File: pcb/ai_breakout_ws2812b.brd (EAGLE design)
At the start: 11.4 x 7.6 mm, 5 parts

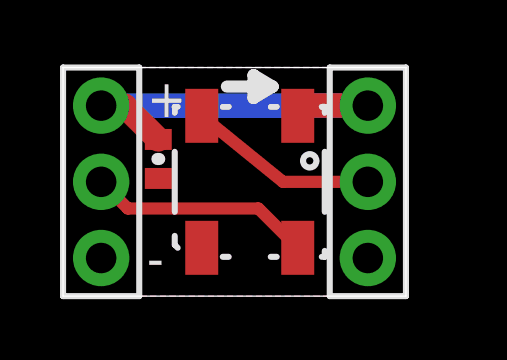
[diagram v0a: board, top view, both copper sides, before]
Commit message: adding panelized version
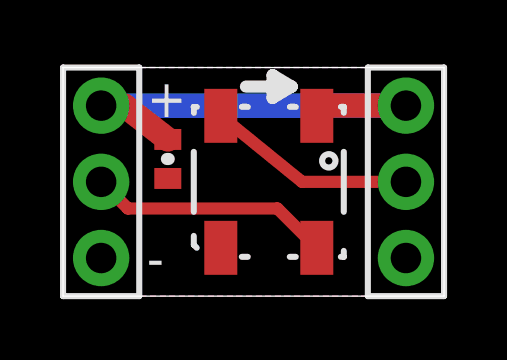
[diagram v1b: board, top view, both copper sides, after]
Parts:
- moved OUT 1.27 mm to (11.4, 3.81)
- moved U$5 0.95 mm to (7.56, 2.67)
- moved RGB 0.63 mm to (6.86, 3.81)
- moved C1 0.32 mm to (3.49, 4.57)
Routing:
- net VCC: track 13.7 -> 15.9 mm
- net DI: track 7.46 -> 8.10 mm
- net DO: track 6.32 -> 6.95 mm
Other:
- board size 11.4 x 7.6 mm -> 12.7 x 7.6 mm
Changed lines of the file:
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@@
 <?xml version="1.0" encoding="utf-8"?>
 <!DOCTYPE eagle SYSTEM "eagle.dtd">
-<eagle version="7.1.0">
+<eagle version="6.5.0">
 <drawing>
 <settings>
@@
 <setting verticaltext="up"/>
 </settings>
-<grid distance="50" unitdist="mil" unit="mil" style="lines" multiple="1" display="yes" altdistance="0.025" altunitdist="inch" altunit="inch"/>
+<grid distance="15" unitdist="mil" unit="mil" style="lines" multiple="1" display="yes" altdistance="0.025" altunitdist="inch" altunit="inch"/>
 <layers>
 <layer number="1" name="Top" color="4" fill="1" visible="yes" active="yes"/>
+<layer number="2" name="Route2" color="1" fill="3" visible="no" active="no"/>
+<layer number="3" name="Route3" color="4" fill="3" visible="no" active="no"/>
+<layer number="4" name="Route4" color="1" fill="4" visible="no" active="no"/>
+<layer number="5" name="Route5" color="4" fill="4" visible="no" active="no"/>
+<layer number="6" name="Route6" color="1" fill="8" visible="no" active="no"/>
+<layer number="7" name="Route7" color="4" fill="8" visible="no" active="no"/>
+<layer number="8" name="Route8" color="1" fill="2" visible="no" active="no"/>
+<layer number="9" name="Route9" color="4" fill="2" visible="no" active="no"/>
+<layer number="10" name="Route10" color="1" fill="7" visible="no" active="no"/>
+<layer number="11" name="Route11" color="4" fill="7" visible="no" active="no"/>
+<layer number="12" name="Route12" color="1" fill="5" visible="no" active="no"/>
+<layer number="13" name="Route13" color="4" fill="5" visible="no" active="no"/>
+<layer number="14" name="Route14" color="1" fill="6" visible="no" active="no"/>
+<layer number="15" name="Route15" color="4" fill="6" visible="no" active="no"/>
 <layer number="16" name="Bottom" color="1" fill="1" visible="yes" active="yes"/>
 <layer number="17" name="Pads" color="2" fill="1" visible="yes" active="yes"/>
@@
 <board>
 <plain>
-<wire x1="0" y1="0" x2="11.43" y2="0" width="0.0254" layer="20"/>
-<wire x1="11.43" y1="0" x2="11.43" y2="7.62" width="0.0254" layer="20"/>
-<wire x1="11.43" y1="7.62" x2="0" y2="7.62" width="0.0254" layer="20"/>
+<wire x1="0" y1="0" x2="12.7" y2="0" width="0.0254" layer="20"/>
+<wire x1="12.7" y1="0" x2="12.7" y2="7.62" width="0.0254" layer="20"/>
+<wire x1="12.7" y1="7.62" x2="0" y2="7.62" width="0.0254" layer="20"/>
 <wire x1="0" y1="7.62" x2="0" y2="0" width="0.0254" layer="20"/>
-<text x="7.62" y="0.127" size="0.635" layer="22" font="vector" ratio="10" rot="SMR0">WS2812B</text>
-<text x="4.572" y="5.842" size="0.635" layer="22" font="vector" ratio="10" rot="MR180">v1.0</text>
+<text x="8.255" y="0.127" size="0.635" layer="22" font="vector" ratio="10" rot="SMR0">WS2812B</text>
+<text x="5.461" y="5.842" size="0.635" layer="22" font="vector" ratio="10" rot="MR180">v1.0</text>
 <text x="2.54" y="4.191" size="0.889" layer="22" font="vector" ratio="10" rot="MR180">DI</text>
 <text x="2.54" y="6.858" size="0.889" layer="22" font="vector" ratio="10" rot="MR180">VCC</text>
-<text x="2.54" y="2.159" size="0.889" layer="22" font="vector" ratio="10" rot="MR180">GND</text>
-<text x="6.223" y="2.159" size="0.889" layer="22" font="vector" ratio="10" rot="MR180">GND</text>
-<text x="6.985" y="4.191" size="0.889" layer="22" font="vector" ratio="10" rot="MR180">DO</text>
-<text x="6.223" y="6.858" size="0.889" layer="22" font="vector" ratio="10" rot="MR180">VCC</text>
-<wire x1="5.461" y1="6.985" x2="6.985" y2="6.985" width="0.4064" layer="21"/>
-<wire x1="6.35" y1="6.604" x2="6.985" y2="6.985" width="0.4064" layer="21"/>
-<wire x1="6.985" y1="6.985" x2="6.35" y2="7.366" width="0.4064" layer="21"/>
-<wire x1="6.35" y1="7.366" x2="6.35" y2="6.604" width="0.4064" layer="21"/>
+<text x="2.54" y="1.8415" size="0.889" layer="22" font="vector" ratio="10" rot="MR180">GND</text>
+<text x="7.493" y="1.8415" size="0.889" layer="22" font="vector" ratio="10" rot="MR180">GND</text>
+<text x="8.255" y="4.191" size="0.889" layer="22" font="vector" ratio="10" rot="MR180">DO</text>
+<text x="7.493" y="6.858" size="0.889" layer="22" font="vector" ratio="10" rot="MR180">VCC</text>
+<wire x1="6.096" y1="6.985" x2="7.62" y2="6.985" width="0.4064" layer="21"/>
+<wire x1="6.985" y1="6.604" x2="7.62" y2="6.985" width="0.4064" layer="21"/>
+<wire x1="7.62" y1="6.985" x2="6.985" y2="7.366" width="0.4064" layer="21"/>
+<wire x1="6.985" y1="7.366" x2="6.985" y2="6.604" width="0.4064" layer="21"/>
 <text x="2.794" y="5.969" size="1.27" layer="21" ratio="10">+</text>
 <text x="2.794" y="0.635" size="1.27" layer="21" ratio="10">-</text>
@@
 <pass name="Default">
 <param name="RoutingGrid" value="50mil"/>
-<param name="AutoGrid" value="1"/>
-<param name="Efforts" value="0"/>
-<param name="TopRouterVariant" value="1"/>
 <param name="tpViaShape" value="round"/>
 <param name="PrefDir.1" value="|"/>
@@
 </autorouter>
 <elements>
-<element name="RGB" library="Ai_LED" package="LED-WS2812B-SM" value="LED-WS2812B-SM" x="6.223" y="3.81" smashed="yes" rot="R270"/>
-<element name="C1" library="Ai_Passives" package="CAP-0402" value="0.1uF" x="3.175" y="4.572" smashed="yes" rot="R270"/>
+<element name="RGB" library="Ai_LED" package="LED-WS2812B-SM" value="LED-WS2812B-SM" x="6.858" y="3.81" smashed="yes" rot="R270"/>
+<element name="C1" library="Ai_Passives" package="CAP-0402" value="0.1uF" x="3.4925" y="4.572" smashed="yes" rot="R270"/>
 <element name="IN" library="Ai_Connectors" package="1X03" value="1X03" x="1.27" y="3.81" smashed="yes" rot="R90"/>
-<element name="OUT" library="Ai_Connectors" package="1X03-NOFIRST" value="1X03NOFIRST" x="10.16" y="3.81" smashed="yes" rot="R90"/>
-<element name="U$5" library="Ai_Miscellany" package="AI-LOGO-XS" value="" x="6.604" y="2.667" rot="MR0"/>
+<element name="OUT" library="Ai_Connectors" package="1X03-NOFIRST" value="1X03NOFIRST" x="11.43" y="3.81" smashed="yes" rot="R90"/>
+<element name="U$5" library="Ai_Miscellany" package="AI-LOGO-XS" value="" x="7.5565" y="2.667" rot="MR0"/>
 </elements>
 <signals>
@@
 <contactref element="OUT" pad="3"/>
 <contactref element="IN" pad="3"/>
-<wire x1="10.16" y1="6.35" x2="1.27" y2="6.35" width="0.8128" layer="16"/>
-<wire x1="7.823" y1="6.01" x2="8.163" y2="6.35" width="0.8128" layer="1"/>
-<wire x1="8.163" y1="6.35" x2="10.16" y2="6.35" width="0.8128" layer="1"/>
-<wire x1="3.175" y1="5.222" x2="2.043" y2="6.35" width="0.8128" layer="1"/>
+<wire x1="11.43" y1="6.35" x2="1.27" y2="6.35" width="0.8128" layer="16"/>
+<wire x1="8.458" y1="6.01" x2="8.798" y2="6.35" width="0.8128" layer="1"/>
+<wire x1="8.798" y1="6.35" x2="11.43" y2="6.35" width="0.8128" layer="1"/>
+<wire x1="3.4925" y1="5.222" x2="2.043" y2="6.35" width="0.8128" layer="1"/>
 <wire x1="2.043" y1="6.35" x2="1.27" y2="6.35" width="0.8128" layer="1"/>
 </signal>
@@
 <polygon width="0.254" layer="1">
 <vertex x="0" y="7.62"/>
-<vertex x="11.43" y="7.62"/>
-<vertex x="11.43" y="0"/>
+<vertex x="12.7" y="7.62"/>
+<vertex x="12.7" y="0"/>
 <vertex x="0" y="0"/>
 </polygon>
 <polygon width="0.254" layer="16">
 <vertex x="0" y="7.62"/>
-<vertex x="11.43" y="7.62"/>
-<vertex x="11.43" y="0"/>
+<vertex x="12.7" y="7.62"/>
+<vertex x="12.7" y="0"/>
 <vertex x="0" y="0"/>
 </polygon>
@@
 <contactref element="RGB" pad="4"/>
 <contactref element="IN" pad="2"/>
-<wire x1="7.823" y1="1.61" x2="6.512" y2="2.921" width="0.4064" layer="1"/>
-<wire x1="6.512" y1="2.921" x2="2.159" y2="2.921" width="0.4064" layer="1"/>
+<wire x1="8.458" y1="1.61" x2="7.147" y2="2.921" width="0.4064" layer="1"/>
+<wire x1="7.147" y1="2.921" x2="2.159" y2="2.921" width="0.4064" layer="1"/>
 <wire x1="2.159" y1="2.921" x2="1.27" y2="3.81" width="0.4064" layer="1"/>
 </signal>
@@
 <contactref element="RGB" pad="2"/>
 <contactref element="OUT" pad="2"/>
-<wire x1="4.623" y1="6.01" x2="7.331" y2="3.81" width="0.4064" layer="1"/>
-<wire x1="7.331" y1="3.81" x2="10.16" y2="3.81" width="0.4064" layer="1"/>
+<wire x1="5.258" y1="6.01" x2="7.966" y2="3.81" width="0.4064" layer="1"/>
+<wire x1="7.966" y1="3.81" x2="11.43" y2="3.81" width="0.4064" layer="1"/>
 </signal>
 </signals>
